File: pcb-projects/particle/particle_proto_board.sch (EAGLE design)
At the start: 37 parts, among them IC1 ATTINY20-MMH, IC2 DMC2400V, IC3 DMC2400V, J1 FTS-103-01-L-DV, SW1 T/S-PI SW, SW2 T/S-PI SW, SW3 T/S-PI SW

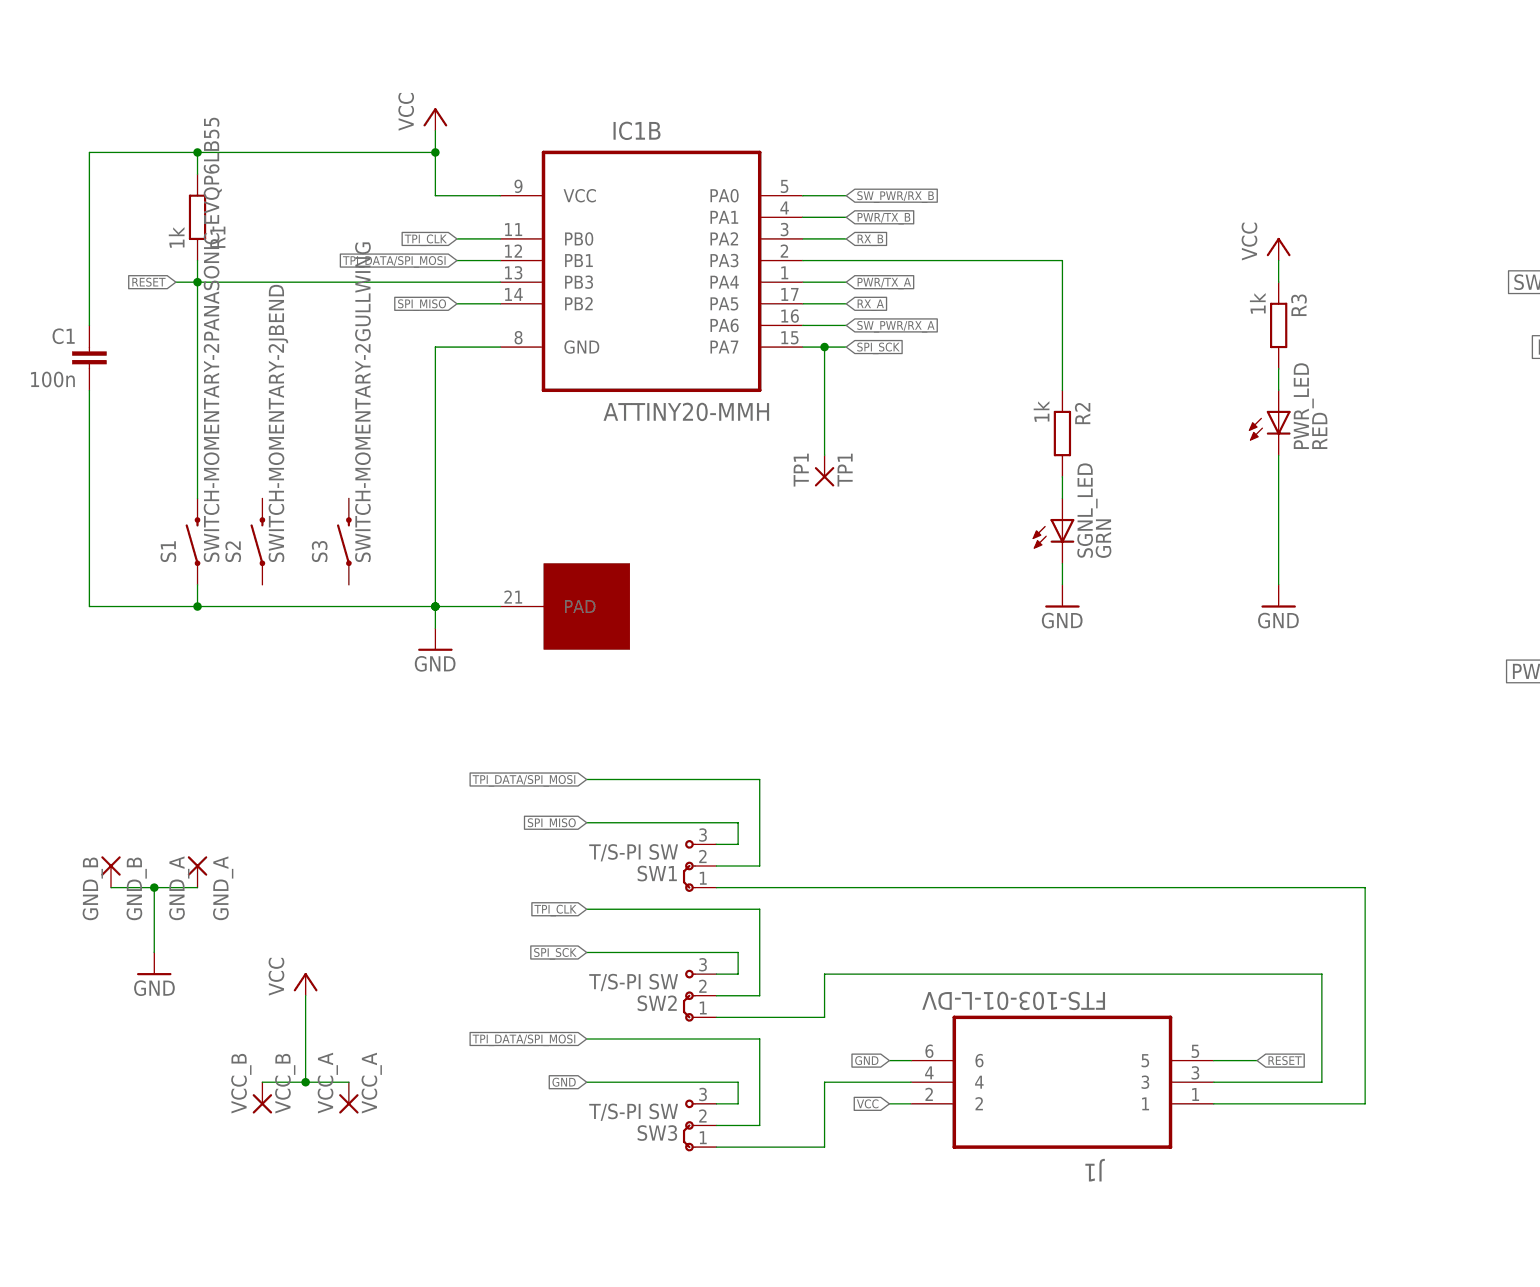
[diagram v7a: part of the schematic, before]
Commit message: routed board with rs components
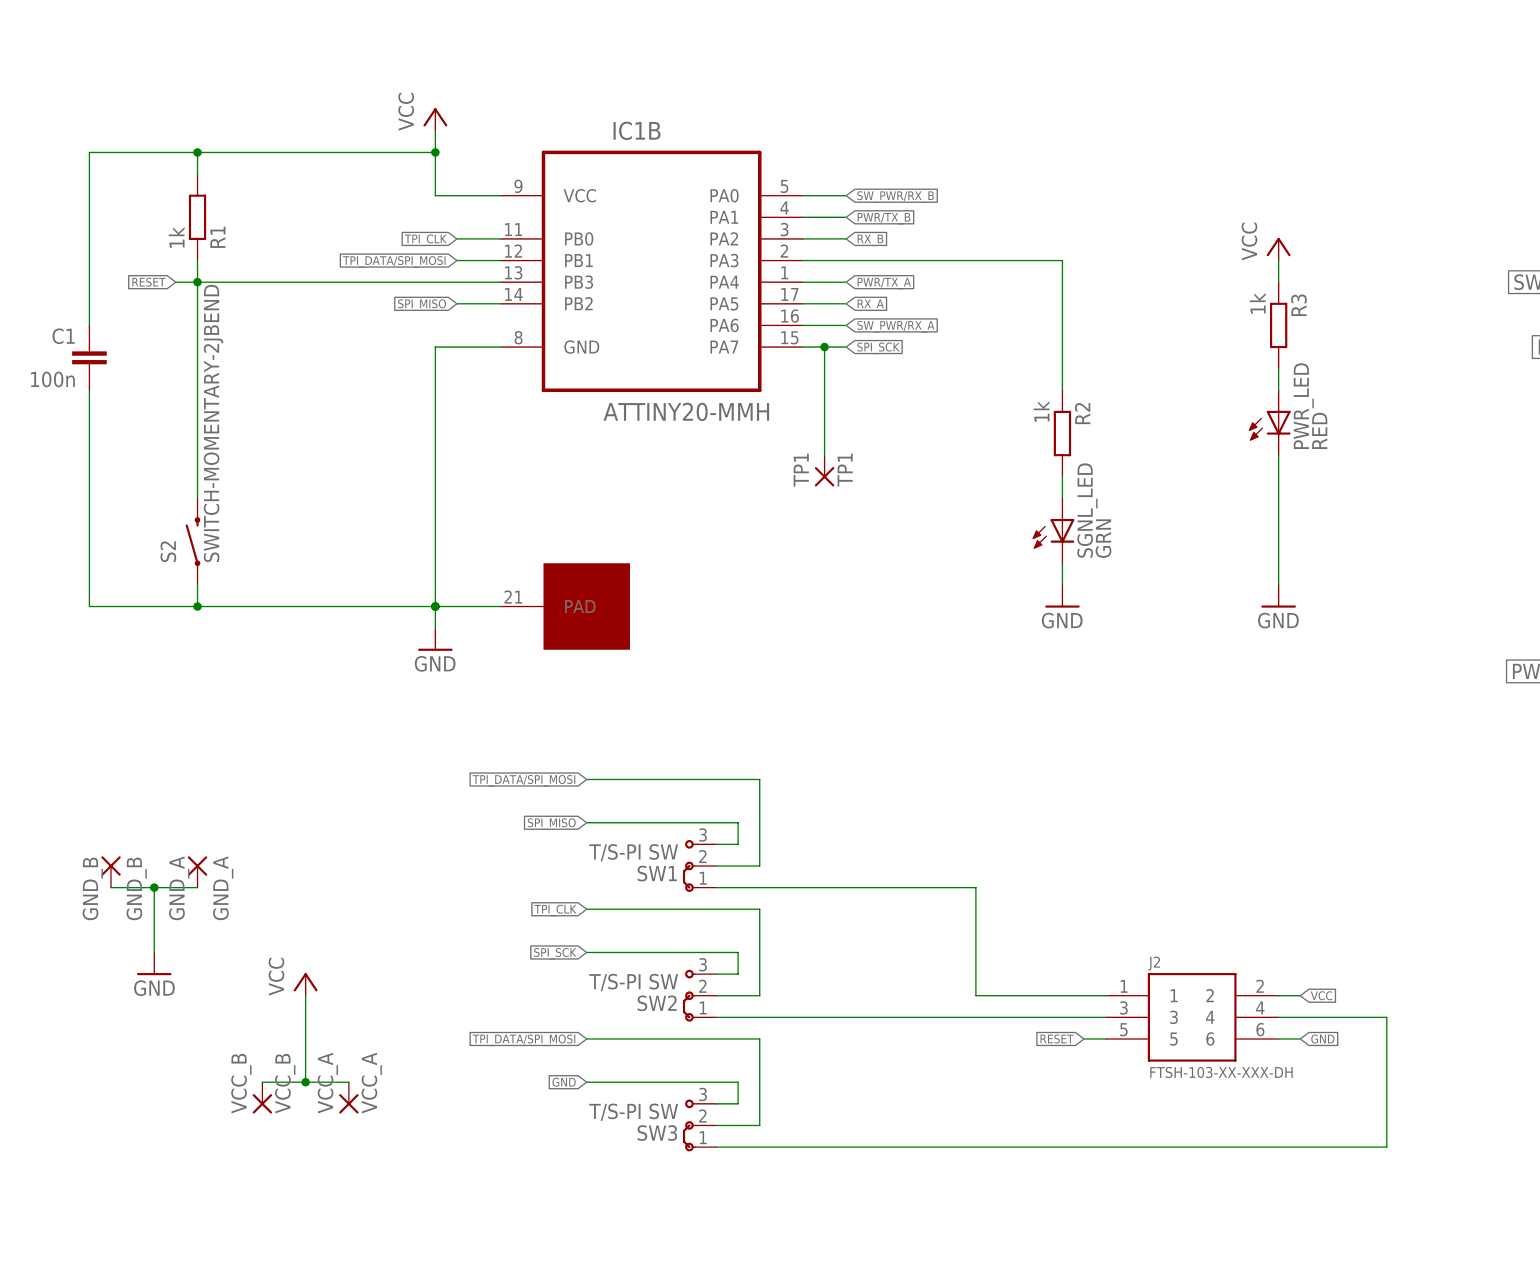
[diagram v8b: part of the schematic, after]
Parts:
- removed J1: FTS-103-01-L-DV, samtec-FTS-103-01-L-DV:FTS-103-01-L-DV
- removed S1: SWITCH-MOMENTARY-2PANASONIC-EVQP6LB55, ck-ksc-switches:SWITCH-MOMENTARY-2PANASONIC-EVQP6LB55
- removed S3: SWITCH-MOMENTARY-2GULLWING, rs-switches:SWITCH-MOMENTARY-2GULLWING
- added J2: FTSH-103-XX-XXX-DH, FTSH-103-XX-XXX-DH:FTSH-103-XX-XXX-DH
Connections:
- net GND: now also J2.6, S2.1; no longer J1.6, S1.1
- net N$1: now also J2.1; no longer J1.1
- net N$15: now also J2.4; no longer J1.4
- net N$20: now also J2.3; no longer J1.3
- net RESET: now also J2.5, S2.2; no longer J1.5, S1.2
- net VCC: now also J2.2; no longer J1.2
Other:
- moved on the sheet: S2
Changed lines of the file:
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@@
 <part name="PWR_LED" library="led" deviceset="LED" device="SML1206" value="RED"/>
 <part name="P+3" library="supply1" deviceset="VCC" device=""/>
-<part name="J1" library="samtec-FTS-103-01-L-DV" deviceset="FTS-103-01-L-DV" device=""/>
 <part name="SW1" library="jumper-switches" deviceset="J2" device="X2MM" value="T/S-PI SW"/>
 <part name="SW3" library="jumper-switches" deviceset="J2" device="X2MM" value="T/S-PI SW"/>
 <part name="SW2" library="jumper-switches" deviceset="J2" device="X2MM" value="T/S-PI SW"/>
-<part name="S1" library="ck-ksc-switches" deviceset="SWITCH-MOMENTARY-2" device="PANASONIC-EVQP6LB55"/>
 <part name="S2" library="rs-switches" deviceset="SWITCH-MOMENTARY-2" device="JBEND"/>
-<part name="S3" library="rs-switches" deviceset="SWITCH-MOMENTARY-2" device="" technology="GULLWING"/>
+<part name="J2" library="FTSH-103-XX-XXX-DH" deviceset="FTSH-103-XX-XXX-DH" device=""/>
 </parts>
 <sheets>
@@
 <instance part="PWR_LED" gate="G$1" x="149.86" y="129.54"/>
 <instance part="P+3" gate="VCC" x="149.86" y="149.86"/>
-<instance part="J1" gate="A" x="124.46" y="48.26" rot="R180"/>
 <instance part="SW1" gate="G$1" x="81.28" y="76.2" rot="R180"/>
 <instance part="SW3" gate="G$1" x="81.28" y="45.72" rot="R180"/>
 <instance part="SW2" gate="G$1" x="81.28" y="60.96" rot="R180"/>
-<instance part="S1" gate="G$1" x="22.86" y="114.3" rot="R90"/>
-<instance part="S2" gate="G$1" x="30.48" y="114.3" rot="R90"/>
-<instance part="S3" gate="G$1" x="40.64" y="114.3" rot="R90"/>
+<instance part="S2" gate="G$1" x="22.86" y="114.3" rot="R90"/>
+<instance part="J2" gate="G$1" x="129.54" y="60.96"/>
 </instances>
 <busses>
@@
 <wire x1="50.8" y1="137.16" x2="58.42" y2="137.16" width="0.1524" layer="91"/>
 <wire x1="22.86" y1="109.22" x2="22.86" y2="106.68" width="0.1524" layer="91"/>
-<pinref part="S1" gate="G$1" pin="1"/>
+<pinref part="S2" gate="G$1" pin="1"/>
 </segment>
 <segment>
@@
 </segment>
 <segment>
-<pinref part="J1" gate="A" pin="6"/>
-<wire x1="106.68" y1="53.34" x2="104.14" y2="53.34" width="0.1524" layer="91"/>
-<label x="104.14" y="53.34" size="1.016" layer="95" rot="R180" xref="yes"/>
+<wire x1="149.86" y1="55.88" x2="152.4" y2="55.88" width="0.1524" layer="91"/>
+<label x="152.4" y="55.88" size="1.016" layer="95" xref="yes"/>
+<pinref part="J2" gate="G$1" pin="6"/>
 </segment>
 <segment>
@@
 <pinref part="IC1" gate="B" pin="PB3"/>
 <wire x1="22.86" y1="144.78" x2="58.42" y2="144.78" width="0.1524" layer="91"/>
-<pinref part="S1" gate="G$1" pin="2"/>
-</segment>
-<segment>
-<pinref part="J1" gate="A" pin="5"/>
-<wire x1="142.24" y1="53.34" x2="147.32" y2="53.34" width="0.1524" layer="91"/>
-<label x="147.32" y="53.34" size="1.016" layer="95" xref="yes"/>
+<pinref part="S2" gate="G$1" pin="2"/>
+</segment>
+<segment>
+<wire x1="129.54" y1="55.88" x2="127" y2="55.88" width="0.1524" layer="91"/>
+<label x="127" y="55.88" size="1.016" layer="95" rot="R180" xref="yes"/>
+<pinref part="J2" gate="G$1" pin="5"/>
 </segment>
 </net>
@@
 </segment>
 <segment>
-<pinref part="J1" gate="A" pin="2"/>
-<wire x1="106.68" y1="48.26" x2="104.14" y2="48.26" width="0.1524" layer="91"/>
-<label x="104.14" y="48.26" size="1.016" layer="95" rot="R180" xref="yes"/>
+<wire x1="149.86" y1="60.96" x2="152.4" y2="60.96" width="0.1524" layer="91"/>
+<label x="152.4" y="60.96" size="1.016" layer="95" xref="yes"/>
+<pinref part="J2" gate="G$1" pin="2"/>
 </segment>
 </net>
@@
 <net name="N$20" class="0">
 <segment>
-<wire x1="83.82" y1="58.42" x2="96.52" y2="58.42" width="0.1524" layer="91"/>
-<wire x1="96.52" y1="58.42" x2="96.52" y2="63.5" width="0.1524" layer="91"/>
-<wire x1="96.52" y1="63.5" x2="154.94" y2="63.5" width="0.1524" layer="91"/>
-<wire x1="154.94" y1="63.5" x2="154.94" y2="50.8" width="0.1524" layer="91"/>
-<pinref part="J1" gate="A" pin="3"/>
-<wire x1="154.94" y1="50.8" x2="142.24" y2="50.8" width="0.1524" layer="91"/>
+<wire x1="83.82" y1="58.42" x2="129.54" y2="58.42" width="0.1524" layer="91"/>
 <pinref part="SW2" gate="G$1" pin="1"/>
+<pinref part="J2" gate="G$1" pin="3"/>
 </segment>
 </net>
 <net name="N$1" class="0">
 <segment>
-<wire x1="160.02" y1="73.66" x2="160.02" y2="48.26" width="0.1524" layer="91"/>
-<pinref part="J1" gate="A" pin="1"/>
-<wire x1="160.02" y1="48.26" x2="142.24" y2="48.26" width="0.1524" layer="91"/>
-<wire x1="160.02" y1="73.66" x2="83.82" y2="73.66" width="0.1524" layer="91"/>
+<wire x1="114.3" y1="73.66" x2="114.3" y2="60.96" width="0.1524" layer="91"/>
+<wire x1="114.3" y1="60.96" x2="129.54" y2="60.96" width="0.1524" layer="91"/>
+<wire x1="114.3" y1="73.66" x2="83.82" y2="73.66" width="0.1524" layer="91"/>
 <pinref part="SW1" gate="G$1" pin="1"/>
+<pinref part="J2" gate="G$1" pin="1"/>
 </segment>
 </net>
@@
 <net name="N$15" class="0">
 <segment>
-<pinref part="J1" gate="A" pin="4"/>
-<wire x1="83.82" y1="43.18" x2="96.52" y2="43.18" width="0.1524" layer="91"/>
-<wire x1="96.52" y1="43.18" x2="96.52" y2="50.8" width="0.1524" layer="91"/>
-<wire x1="96.52" y1="50.8" x2="106.68" y2="50.8" width="0.1524" layer="91"/>
 <pinref part="SW3" gate="G$1" pin="1"/>
-</segment>
-</net>
+<wire x1="83.82" y1="43.18" x2="162.56" y2="43.18" width="0.1524" layer="91"/>
+<wire x1="162.56" y1="43.18" x2="162.56" y2="58.42" width="0.1524" layer="91"/>
+<pinref part="J2" gate="G$1" pin="4"/>
+<wire x1="162.56" y1="58.42" x2="149.86" y2="58.42" width="0.1524" layer="91"/>
+</segment>
+</net>
